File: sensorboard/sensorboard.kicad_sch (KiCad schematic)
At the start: 63 parts, among them J10 Conn_01x02_Male, J11 Conn_01x05_Male, J15 Conn_Coaxial, J9 Conn_01x02_Male, Q1 MMDT2222A, U1 ESP32-PICO-D4, U2 LTC4411, U3 TPS61092RSAR

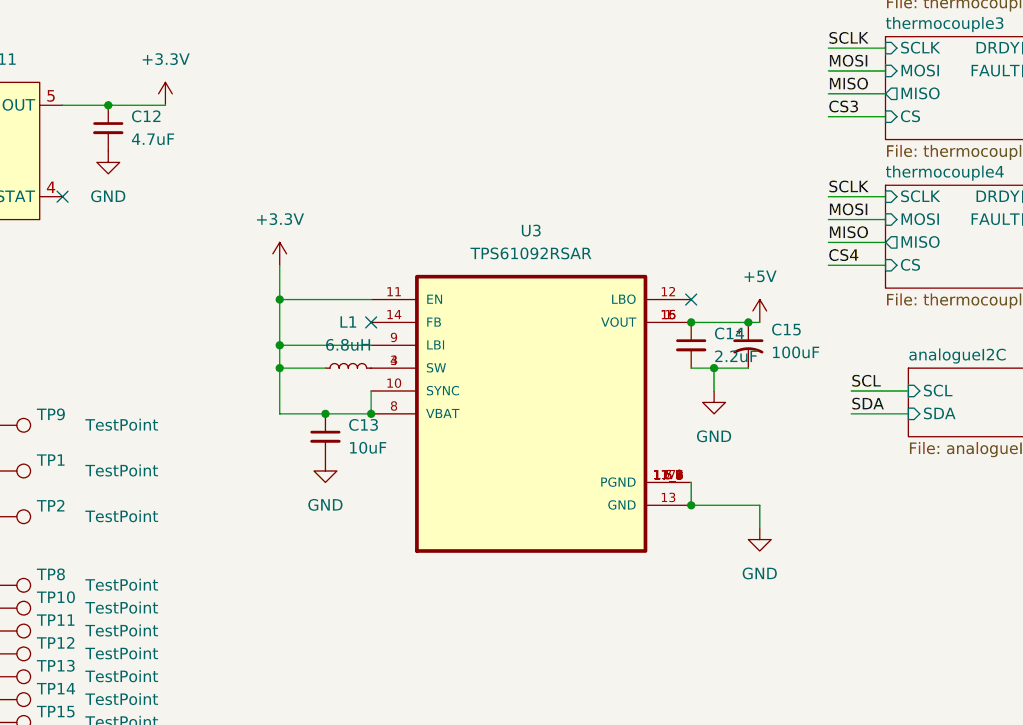
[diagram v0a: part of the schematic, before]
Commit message: updated boost converter schematic, 5V lines
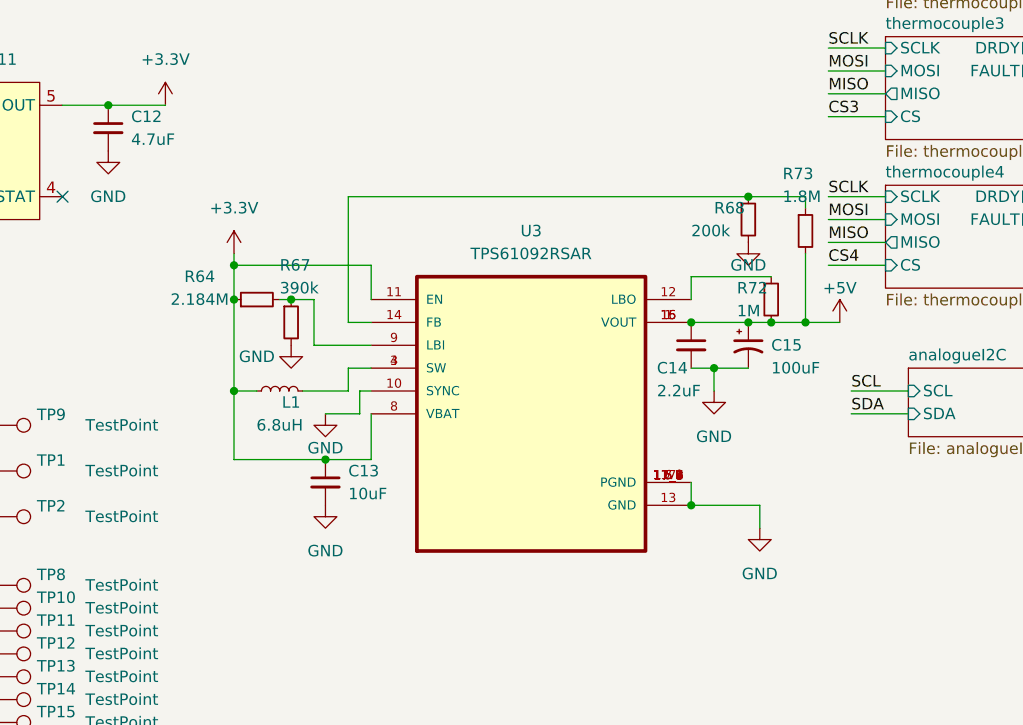
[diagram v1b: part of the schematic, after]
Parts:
- added R64: 2.184M, Resistor_SMD:R_0603_1608Metric, symbol Device:R_Small
- added R67: 390k, Resistor_SMD:R_0603_1608Metric, symbol Device:R_Small
- added R68: 200k, Resistor_SMD:R_0603_1608Metric, symbol Device:R_Small
- added R72: 1M, Resistor_SMD:R_0603_1608Metric, symbol Device:R_Small
- added R73: 1.8M, Resistor_SMD:R_0603_1608Metric, symbol Device:R_Small
- C15: footprint Capacitor_SMD:C_0603_1608Metric -> iclr:CAPC2012X145N
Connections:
- net +3V3: now also R64.1; no longer U3.10 (SYNC), U3.9 (LBI)
- net +5V: now also R72.2, R73.2
- net GND: now also U3.10 (SYNC), R67.2, R68.2
- net at U3.12 (LBO): now also R72.1
- net at U3.14 (FB): now also R68.1, R73.1
- new net: R64.2, R67.1, U3.9 (LBI)
- no-connect marks 37 -> 35
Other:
- moved on the sheet: C13, L1

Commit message: rearranged CAN and boost converter
LEDs moved
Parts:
- L1: footprint iclr:INDC1006X60N -> iclr:INDPM3030X200N
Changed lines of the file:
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@@
     (property "Reference" "L1" (id 0) (at 166.37 113.03 90))
     (property "Value" "6.8uH" (id 1) (at 165.1 115.57 90))
-    (property "Footprint" "iclr:INDC1006X60N" (id 2) (at 165.1 111.76 0)
+    (property "Footprint" "iclr:INDPM3030X200N" (id 2) (at 165.1 111.76 0)
       (effects (font (size 1.27 1.27)) hide)
     )
@@
     )
     (path "/ad46cd95-f162-4a6c-8925-7b744d994db1"
-      (reference "L1") (unit 1) (value "6.8uH") (footprint "iclr:INDC1006X60N")
+      (reference "L1") (unit 1) (value "6.8uH") (footprint "iclr:INDPM3030X200N")
     )
     (path "/00000000-0000-0000-0000-00005e4f19d5"

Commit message: boost converter fixed
rearrangement of coaxial connector line and gnd stitching
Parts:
- added C4: 4.7uF, Capacitor_SMD:C_0603_1608Metric, symbol Device:C_Small
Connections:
- net GND: now also C4.2
- net at J11.3 (Pin_3), U2.1 (IN): now also C4.1
- net USB_DET renamed VBUS
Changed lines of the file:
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@@
   (junction (at 113.03 101.6) (diameter 0) (color 0 0 0 0)
   )
+  (junction (at 114.3 80.01) (diameter 0) (color 0 0 0 0)
+  )
   (junction (at 166.37 101.6) (diameter 0) (color 0 0 0 0)
   )
@@
     (stroke (width 0) (type default) (color 0 0 0 0))
   )
-  (wire (pts (xy 80.01 25.4) (xy 71.12 25.4))
+  (wire (pts (xy 76.2 25.4) (xy 71.12 25.4))
     (stroke (width 0) (type default) (color 0 0 0 0))
   )
@@
     (effects (font (size 1.27 1.27)) (justify right bottom))
   )
-  (label "USB_DET" (at 80.01 25.4 180)
-    (effects (font (size 1.27 1.27)) (justify right bottom))
-  )
   (label "SCLK" (at 254 73.66 0)
     (effects (font (size 1.27 1.27)) (justify left bottom))
@@
     (pin "1")
   )
+  (symbol (lib_id "power:GND") (at 114.3 85.09 0) (unit 1)
+    (in_bom yes) (on_board yes) (fields_autoplaced)
+    (property "Reference" "#PWR022" (id 0) (at 114.3 91.44 0)
+      (effects (font (size 1.27 1.27)) hide)
+    )
+    (property "Value" "GND" (id 1) (at 114.3 90.17 0))
+    (property "Footprint" "" (id 2) (at 114.3 85.09 0)
+      (effects (font (size 1.27 1.27)) hide)
+    )
+    (property "Datasheet" "" (id 3) (at 114.3 85.09 0)
+      (effects (font (size 1.27 1.27)) hide)
+    )
+    (pin "1")
+  )
   (symbol (lib_id "power:GND") (at 213.36 111.76 0) (unit 1)
     (in_bom yes) (on_board yes) (fields_autoplaced)
@@
     (pin "1")
   )
+  (symbol (lib_id "Device:C_Small") (at 114.3 82.55 0) (unit 1)
+    (in_bom yes) (on_board yes) (fields_autoplaced)
+    (property "Reference" "C4" (id 0) (at 116.84 81.2862 0)
+      (effects (font (size 1.27 1.27)) (justify left))
+    )
+    (property "Value" "4.7uF" (id 1) (at 116.84 83.8262 0)
+      (effects (font (size 1.27 1.27)) (justify left))
+    )
+    (property "Footprint" "Capacitor_SMD:C_0603_1608Metric" (id 2) (at 114.3 82.55 0)
+      (effects (font (size 1.27 1.27)) hide)
+    )
+    (property "Datasheet" "~" (id 3) (at 114.3 82.55 0)
+      (effects (font (size 1.27 1.27)) hide)
+    )
+    (pin "1")
+    (pin "2")
+  )
   (symbol (lib_id "Connector:TestPoint") (at 43.18 85.09 270) (unit 1)
     (in_bom yes) (on_board yes) (fields_autoplaced)
@@
     (pin "1")
   )
+  (symbol (lib_id "power:VBUS") (at 76.2 25.4 0) (unit 1)
+    (in_bom yes) (on_board yes)
+    (property "Reference" "#PWR0159" (id 0) (at 76.2 29.21 0)
+      (effects (font (size 1.27 1.27)) hide)
+    )
+    (property "Value" "VBUS" (id 1) (at 76.581 22.1488 90)
+      (effects (font (size 1.27 1.27)) (justify left))
+    )
+    (property "Footprint" "" (id 2) (at 76.2 25.4 0)
+      (effects (font (size 1.27 1.27)) hide)
+    )
+    (property "Datasheet" "" (id 3) (at 76.2 25.4 0)
+      (effects (font (size 1.27 1.27)) hide)
+    )
+    (pin "1")
+  )
   (symbol (lib_id "Connector:TestPoint") (at 80.01 110.49 90) (unit 1)
     (in_bom yes) (on_board yes)
@@
       (reference "#PWR021") (unit 1) (value "GND") (footprint "")
     )
+    (path "/3e8d5184-1816-49eb-9adb-60f410dc0d52"
+      (reference "#PWR022") (unit 1) (value "GND") (footprint "")
+    )
     (path "/00000000-0000-0000-0000-000061cb93b1/00000000-0000-0000-0000-00006199decf"
       (reference "#PWR024") (unit 1) (value "GND") (footprint "")
@@
       (reference "#PWR0158") (unit 1) (value "GND") (footprint "")
     )
+    (path "/9b6c2cec-a0ae-45f2-9100-915244cd8aad"
+      (reference "#PWR0159") (unit 1) (value "VBUS") (footprint "")
+    )
     (path "/00000000-0000-0000-0000-00005dabbfe7"
       (reference "C1") (unit 1) (value "1uF") (footprint "Capacitor_SMD:C_0603_1608Metric")
@@
       (reference "C3") (unit 1) (value "1uF") (footprint "Capacitor_SMD:C_0603_1608Metric")
     )
+    (path "/65644a17-b91f-494c-9bed-79c314a5de15"
+      (reference "C4") (unit 1) (value "4.7uF") (footprint "Capacitor_SMD:C_0603_1608Metric")
+    )
     (path "/00000000-0000-0000-0000-000061cb93b1/00000000-0000-0000-0000-00006199d7ef"

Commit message: Changed pins for CAN lines and removed LED
need to rearrange LNA_IN line for less interference
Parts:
- removed D4: LED, LED_SMD:LED_0603_1608Metric, symbol Device:LED
- removed R12: 470, Resistor_SMD:R_0603_1608Metric, symbol Device:R_Small
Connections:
- net LED is gone; now on net CAN_TX: U1.12 (IO32)
- net CAN_RX: now also U1.13 (IO33); no longer U1.25 (IO16)
- net CAN_TX: no longer U1.27 (IO17)
- net CS3: now also U1.28 (SD2/IO9); no longer U1.22 (IO2)
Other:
- moved on the sheet: TP1, TP22, TP23

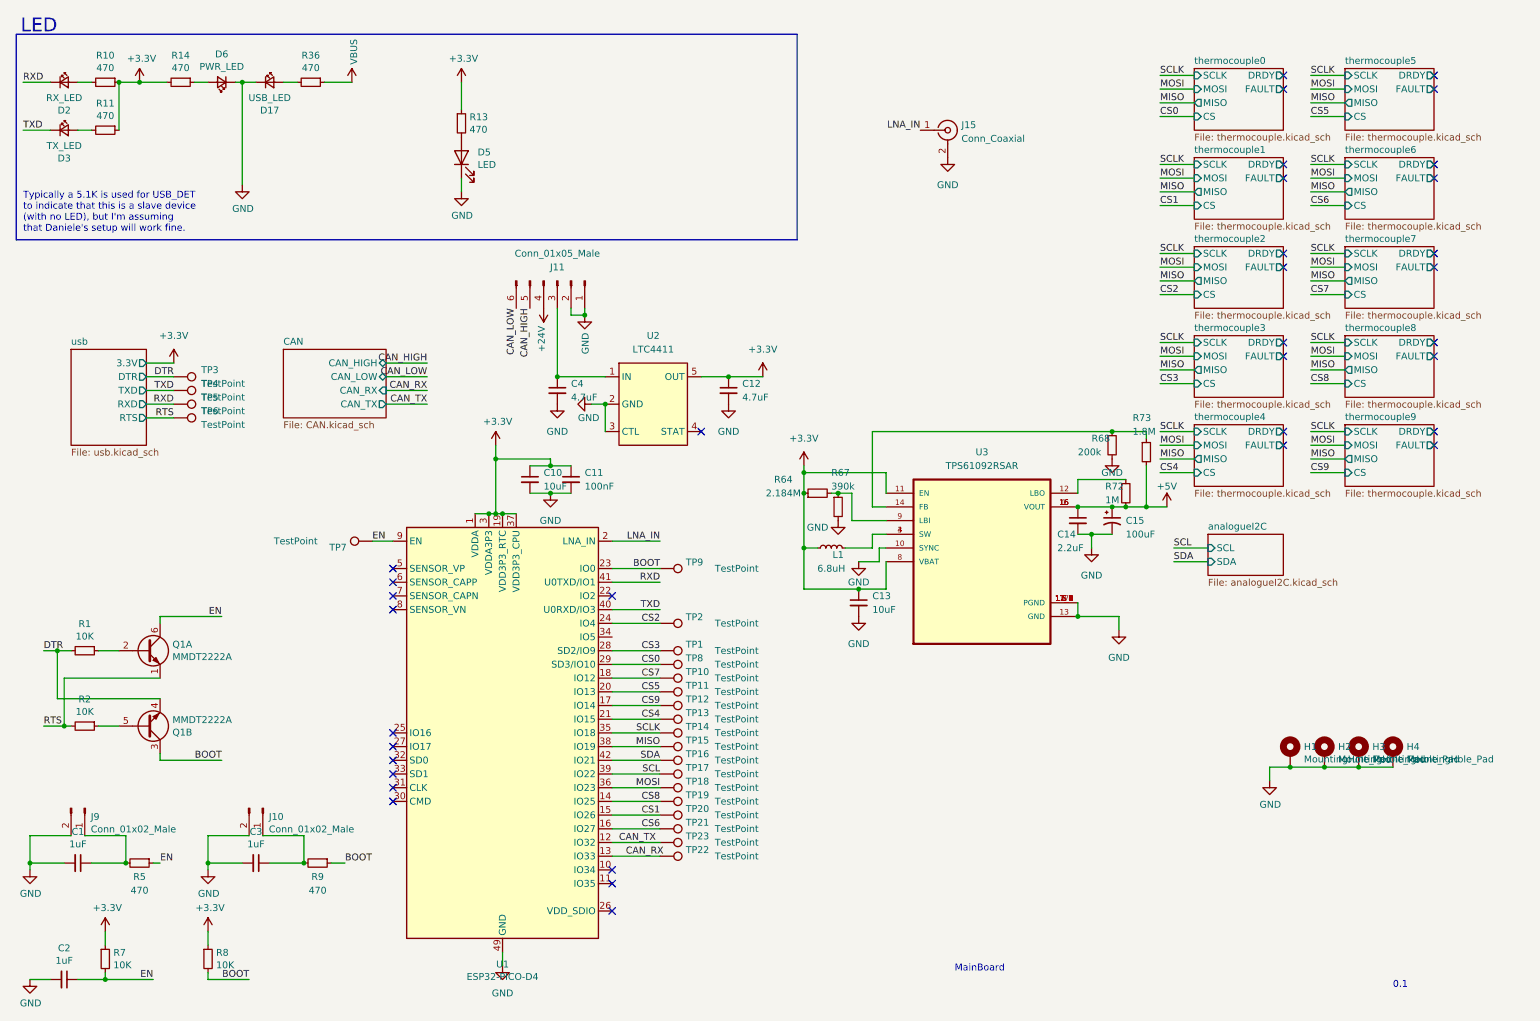
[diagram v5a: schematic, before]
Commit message: added silkscreens and fixed LNA_IN line
fixed labels for TPs and LEDs
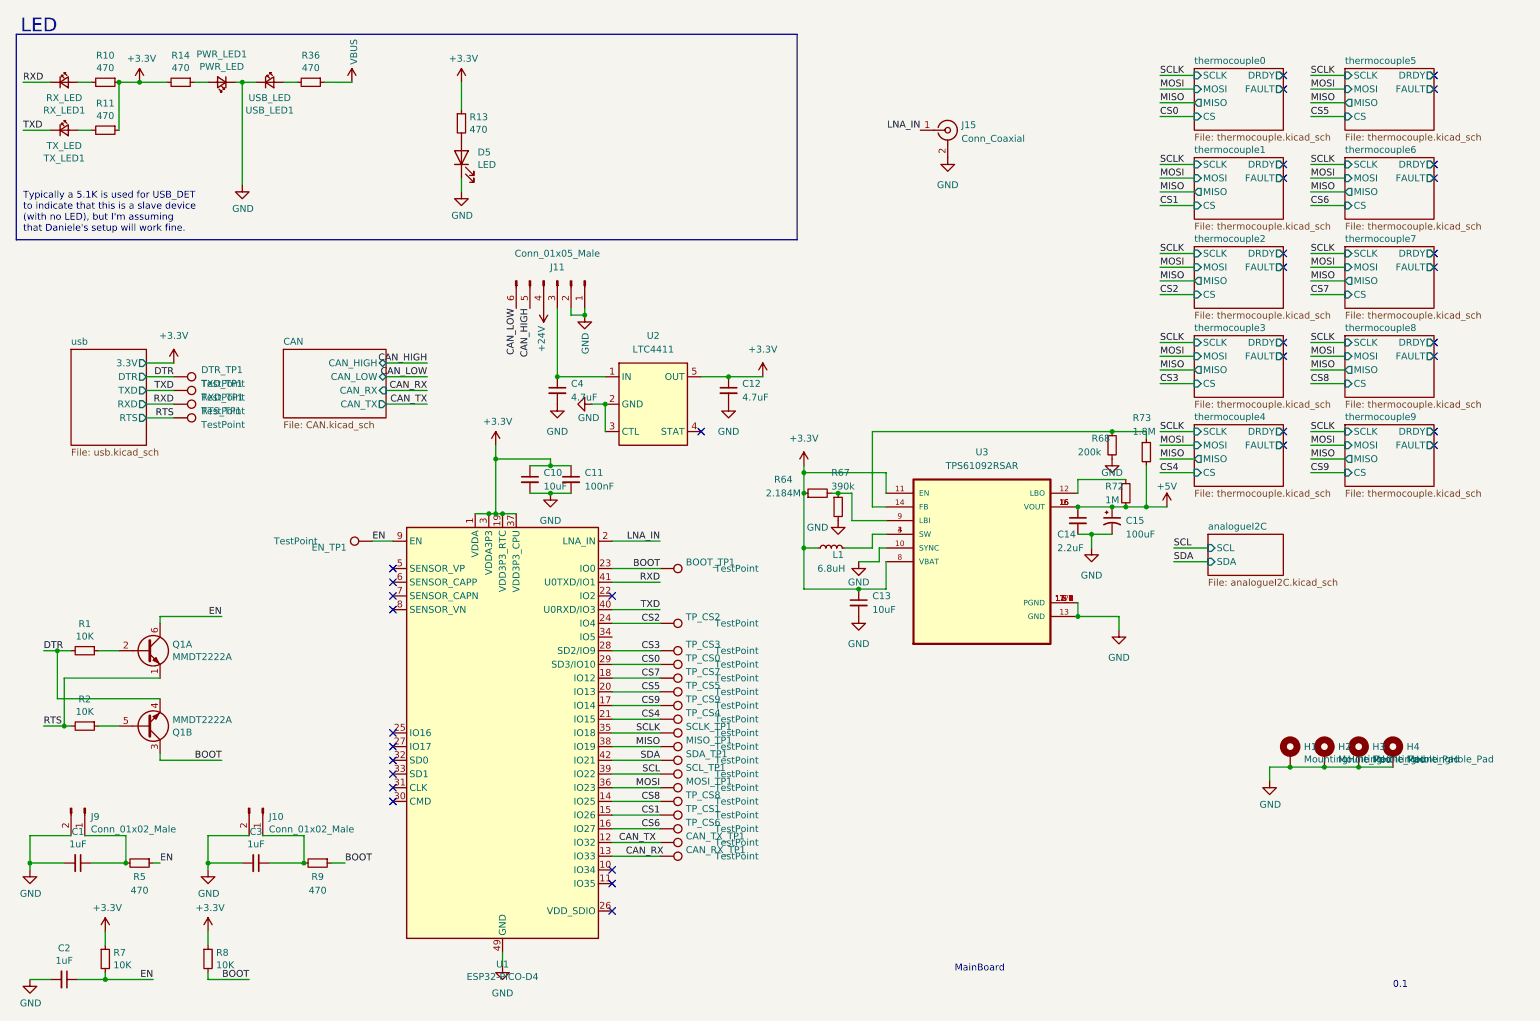
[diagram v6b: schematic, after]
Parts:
- renumbered TP9 to BOOT_TP1, TP22 to CAN_RX_TP1, TP23 to CAN_TX_TP1, TP3 to DTR_TP1, TP7 to EN_TP1, TP15 to MISO_TP1, TP18 to MOSI_TP1, D6 to PWR_LED1, TP6 to RTS_TP1, TP5 to RXD_TP1, D2 to RX_LED1, TP14 to SCLK_TP1, TP17 to SCL_TP1, TP16 to SDA_TP1, TP8 to TP_CS0, TP20 to TP_CS1, TP2 to TP_CS2, TP1 to TP_CS3, TP13 to TP_CS4, TP11 to TP_CS5, TP21 to TP_CS6, TP10 to TP_CS7, TP19 to TP_CS8, TP12 to TP_CS9, TP4 to TXD_TP1, D3 to TX_LED1, D17 to USB_LED1
